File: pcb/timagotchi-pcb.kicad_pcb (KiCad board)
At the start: 2 copper layers, 8 parts, among them SW1 SW_Push, SW2 SW_Push, SW3 SW_Push, U1 Arduino_Nano

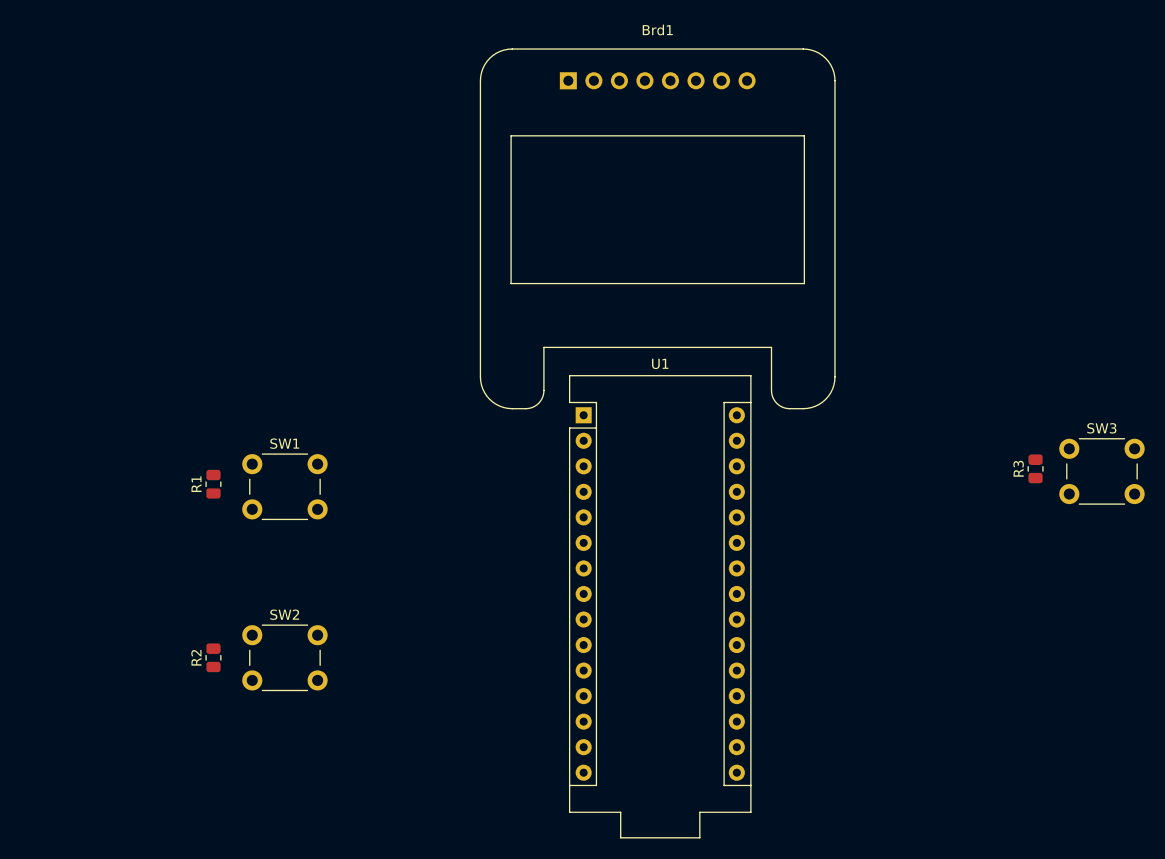
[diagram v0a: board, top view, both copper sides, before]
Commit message: balance resistors and gen new pcb
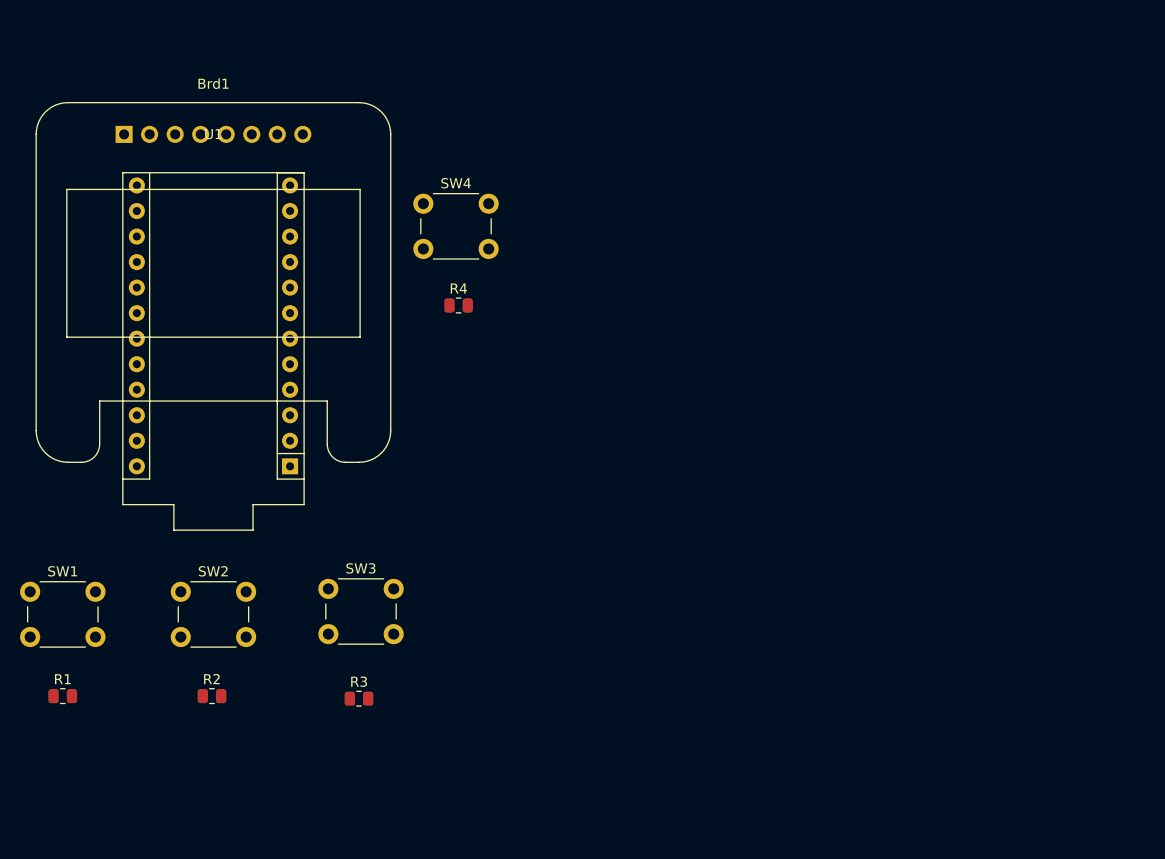
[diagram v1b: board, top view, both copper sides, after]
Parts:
- added R4: 3.3k, Resistor_SMD:R_0805_2012Metric, F.Cu at (172.5, 86.6)
- added SW4: SW_Push, Button_Switch_THT:SW_PUSH_6mm, F.Cu at (169.0, 76.5)
- R1, R2: value 10k -> 3.3k
- U1: value Arduino_Nano -> Sparkfun_Pro_Micro; footprint Arduino:Arduino_Nano -> Arduino:Sparkfun_Pro_Micro
- moved SW3 75.0 mm to (159.5, 114.8)
- moved R3 71.1 mm to (162.6, 125.7), turned to 0 degrees
- moved U1 50.0 mm to (140.5, 74.7)
- moved Brd1 44.5 mm to (139.2, 69.6)
- moved R1 25.9 mm to (133.1, 125.5), turned to 0 degrees
- moved SW1 25.5 mm to (129.8, 115.1)
- moved SW2 8.32 mm to (144.8, 115.1)
- moved R2 3.81 mm to (147.9, 125.5), turned to 0 degrees
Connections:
- Brd1 pad 1: GND -> -BATT
- Brd1 pad 2: +5V -> VCC
- R1 pad 1: Net-(U1-Pad6) -> Net-(R1-Pad1)
- R1 pad 2: GND -> VCC
- R2 pad 1: Net-(U1-Pad7) -> Net-(R2-Pad1)
- R2 pad 2: GND -> VCC
- R3 pad 1: +5V -> Net-(R3-Pad1)
- R3 pad 2: Net-(R3-Pad2) -> VCC
- SW1 pad 1: Net-(U1-Pad6) -> Net-(R1-Pad1)
- SW1 pad 2: +5V -> -BATT
- SW2 pad 1: Net-(U1-Pad7) -> Net-(R2-Pad1)
- SW2 pad 2: +5V -> -BATT
- SW3 pad 1: Net-(R3-Pad2) -> Net-(R3-Pad1)
- SW3 pad 2: GND -> -BATT
- U1 pad 17: unconnected-(U1-Pad17) -> Net-(R3-Pad1)
- U1 pad 18: unconnected-(U1-Pad18) -> Net-(R2-Pad1)
- U1 pad 19: unconnected-(U1-Pad19) -> Net-(R1-Pad1)
- U1 pad 21: unconnected-(U1-Pad21) -> VCC
- U1 pad 22: unconnected-(U1-Pad22) -> Net-(R4-Pad2)
- U1 pad 23: Net-(Brd1-Pad4) -> -BATT
- U1 pad 24: Net-(Brd1-Pad3) -> +BATT
- U1 pad 4: GND -> unconnected-(U1-Pad4)
- U1 pad 5: unconnected-(U1-Pad5) -> Net-(Brd1-Pad4)
- U1 pad 6: Net-(U1-Pad6) -> Net-(Brd1-Pad3)
- U1 pad 7: Net-(U1-Pad7) -> unconnected-(U1-Pad7)
